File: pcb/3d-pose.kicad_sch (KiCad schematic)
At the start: 15 parts, among them U2 TS4231, U3 BNO055, U6 TS4231

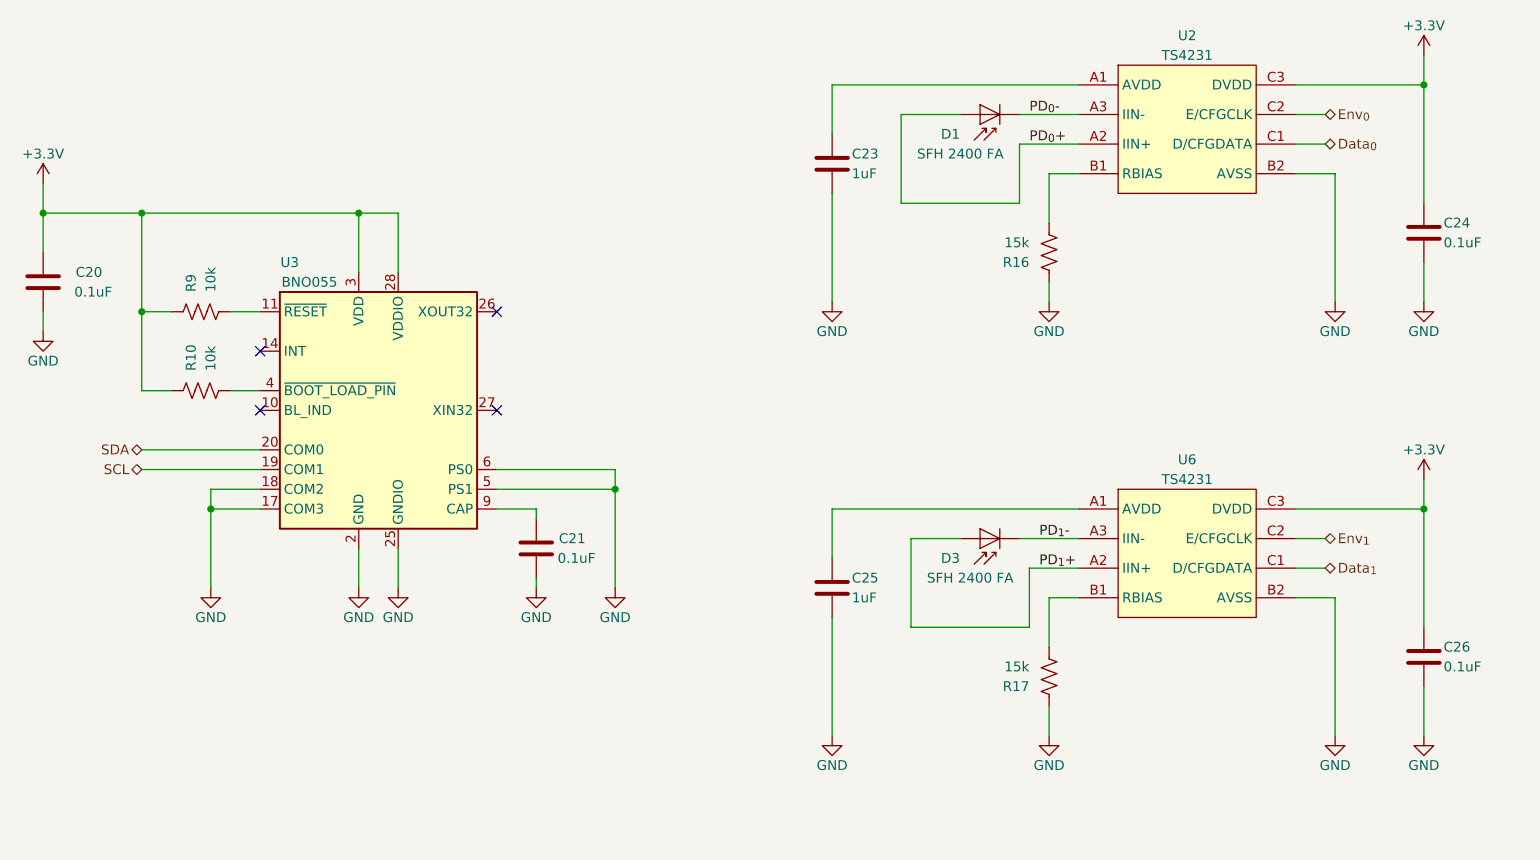
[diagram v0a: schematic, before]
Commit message: Start of revision B
- Address the following issues
1. The photodiode anode is on pin 3, not pin 2
2. No paste on coax connector
3. CRESET_B needs to come out to programming header
4. Need PU on CS line.
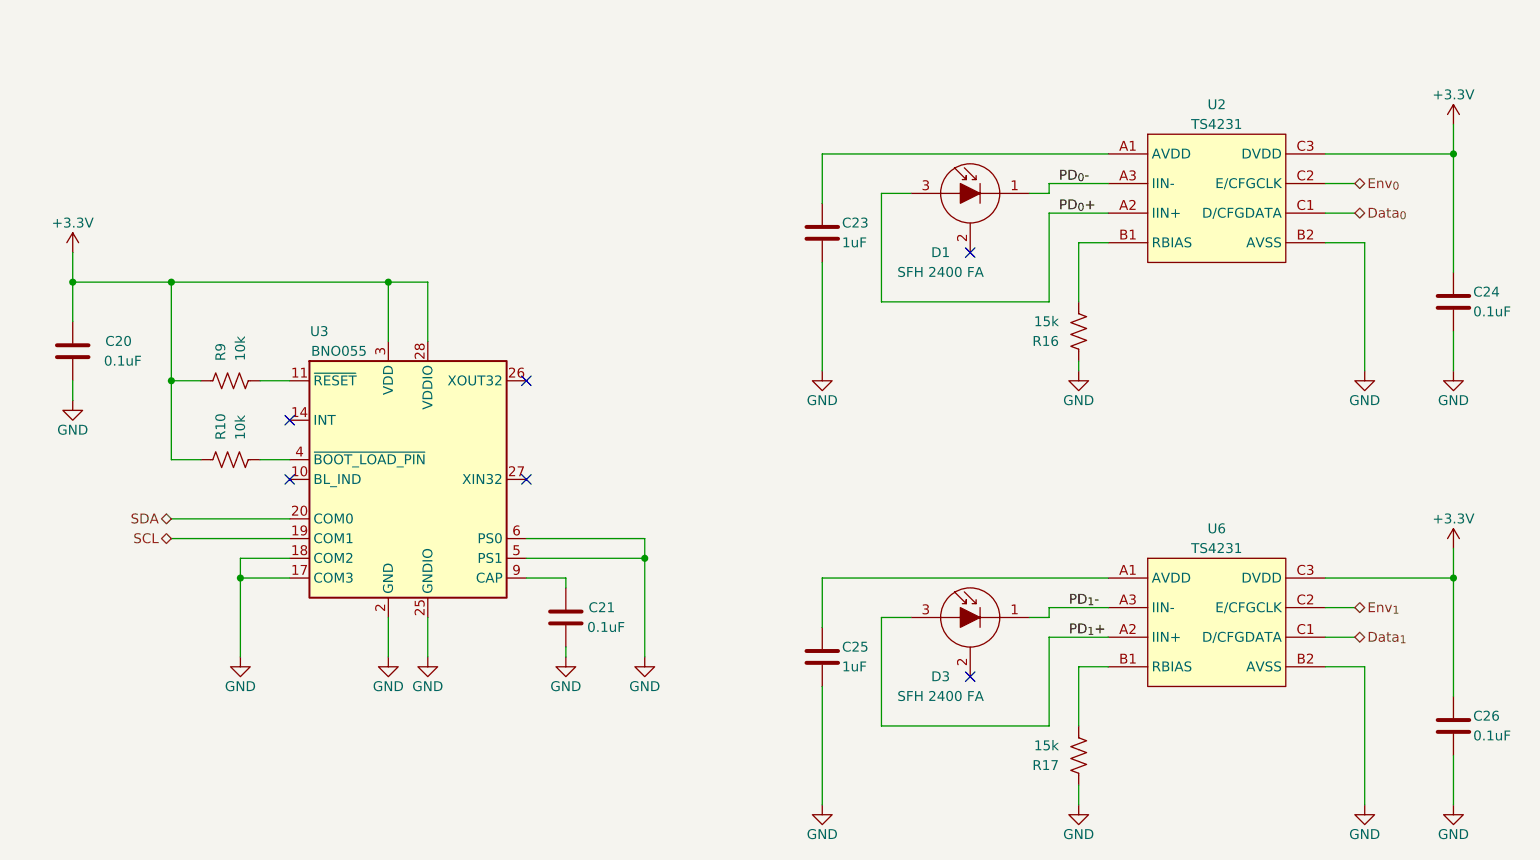
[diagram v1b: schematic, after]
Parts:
- removed D1, D3: SFH 2400 FA, jonnew:OSRAM_SFH2400FA-Tight, symbol Sensor_Optical:BP104-SMD
- added D1, D3: SFH 2400 FA, jonnew:OSRAM_SFH2400FA-Tight, symbol Sensor_Optical:S5973
- C20, C21, C24, C26: TempCo (none) -> X7R; Voltage (none) -> 16V
- C23, C25: TempCo (none) -> X5R; Voltage (none) -> 16V
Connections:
- net PD_{0}+: now also D1.3 (A)
- net PD_{0}-: now also D1.1 (K)
- net PD_{1}+: now also D3.3 (A)
- net PD_{1}-: now also D3.1 (K)
- no-connect marks 4 -> 6
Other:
- title: Kiloscope -> Headstage-64s
- moved on the sheet: C20, C21, C23, C24, C25, C26, R10, R16, R17, R9, U2, U3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
